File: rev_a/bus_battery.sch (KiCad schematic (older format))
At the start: 4 parts

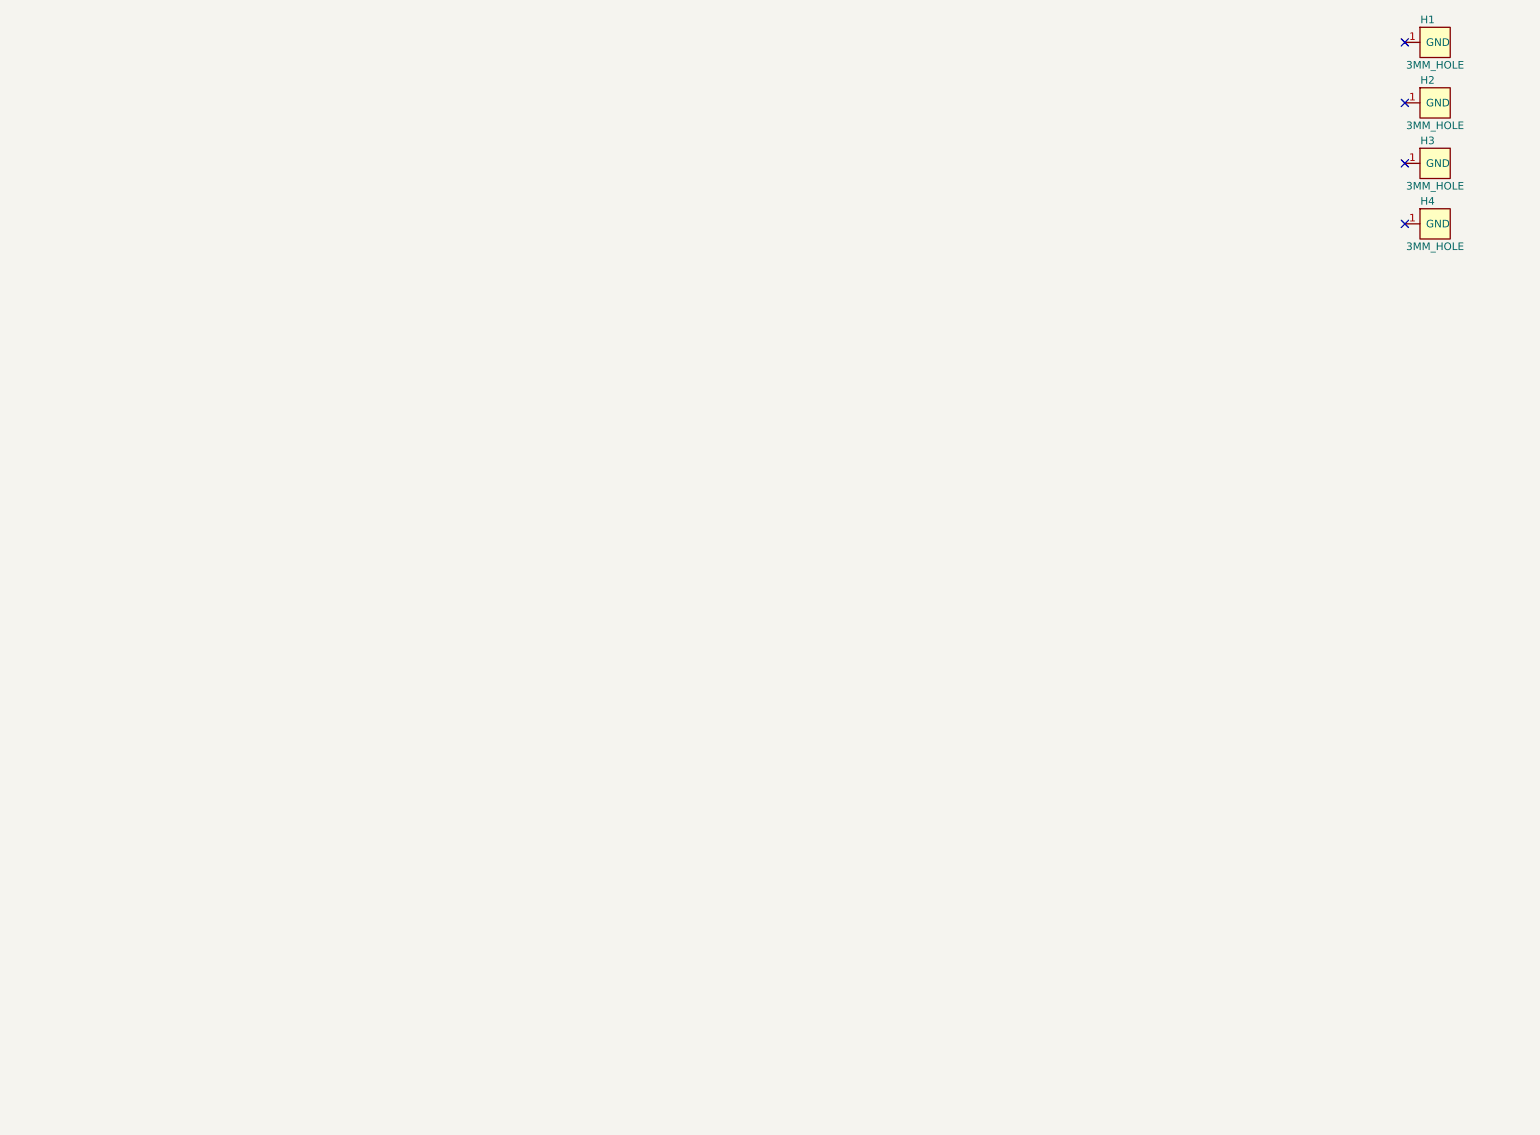
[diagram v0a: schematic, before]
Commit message: Concluded that this will have to be a 5cm x 10cm board.
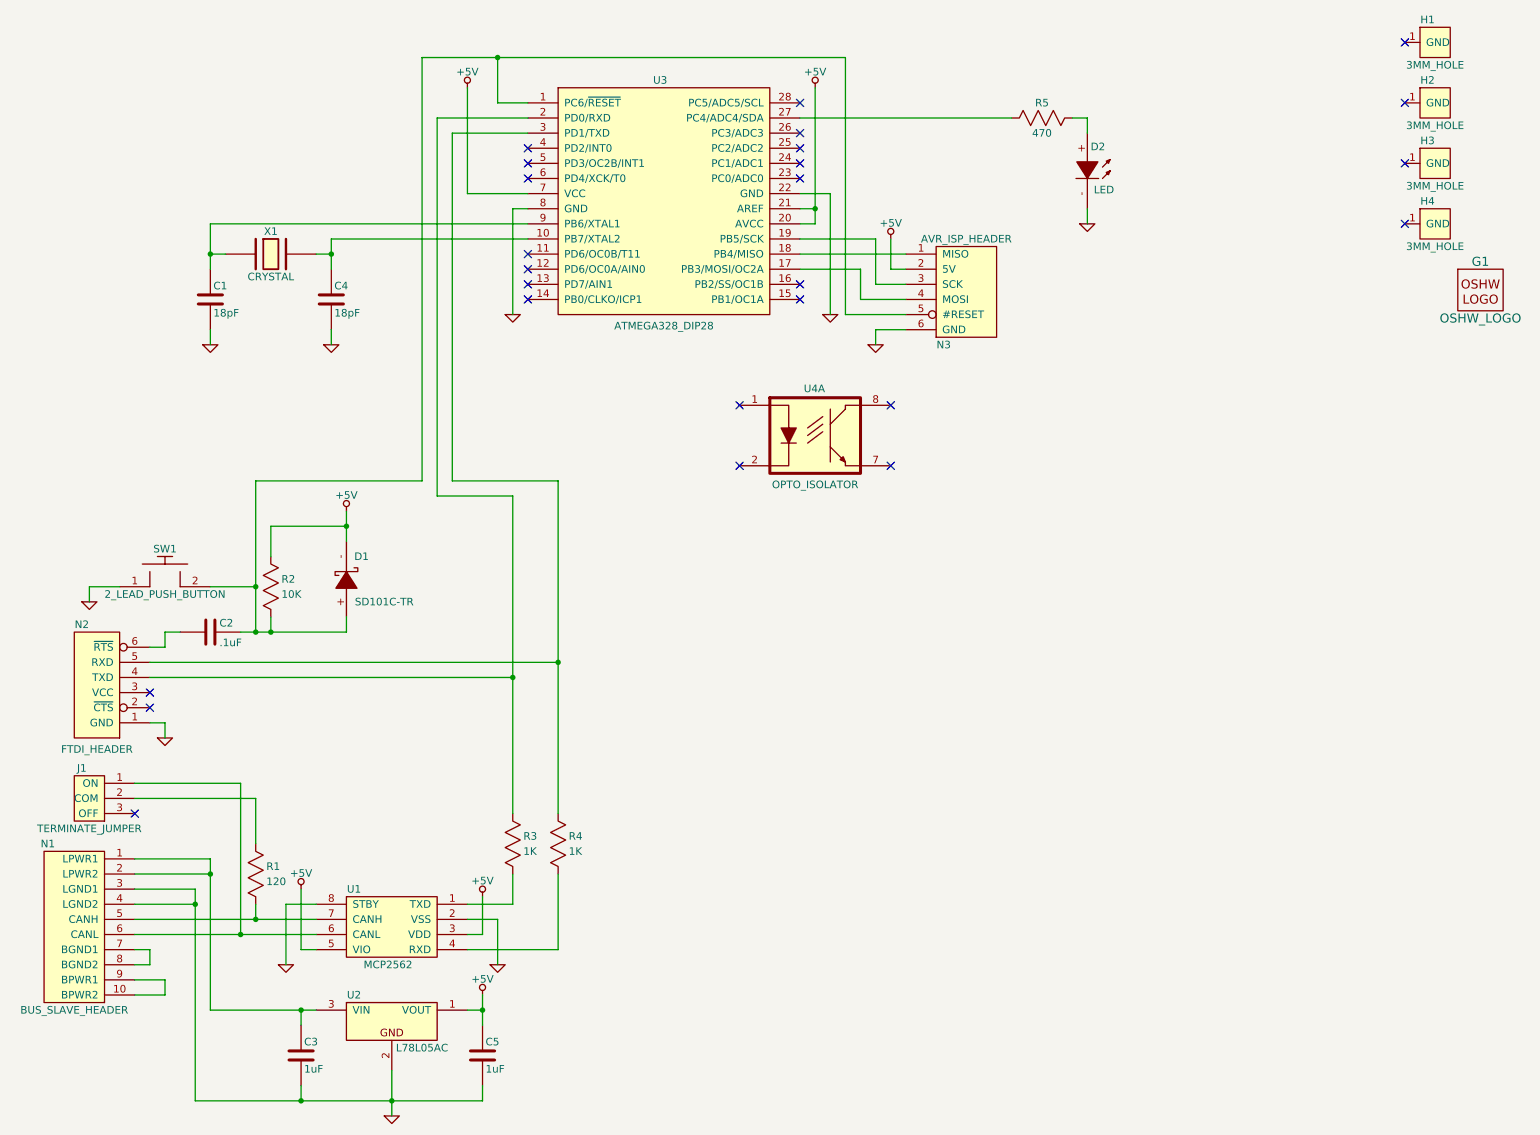
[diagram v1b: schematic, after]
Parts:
- added C1, C4: 18pF, Bus_Battery:Capacitor3MMDiscRM2.5, symbol C_VERT
- added C2: .1uF, Bus_Battery:Capacitor3MMDiscRM2.5, symbol C_HORIZ
- added C3, C5: 1uF, Bus_Battery:Capacitor3MMDiscRM2.5, symbol C_VERT
- added D1: SD101C-TR, Bus_Battery:Diode_DO-41_SOD81_Horizontal_RM10, symbol SCHOTTKY_DIODE_VERT
- added D2: LED, Bus_Battery:T1_LED, symbol LED
- added G1: OSHW_LOGO, Bus_Battery:OSHW_LOGO_250mil, symbol OSHW_LOGO
- added J1: TERMINATE_JUMPER, Bus_Battery:Pin_Header_Straight_1x03, symbol TERMINATE_JUMPER
- added N1: BUS_SLAVE_HEADER, Bus_Battery:Pin_Header_Straight_2x05_Shrouded, symbol BUS_SLAVE_HEADER
- added N2: FTDI_HEADER, Bus_Battery:Pin_Header_Straight_1x06, symbol FTDI_HEADER
- added N3: AVR_ISP_HEADER, Bus_Battery:Pin_Header_Straight_2x03, symbol AVR_ISP_HEADER
- added R1: 120, Bus_Battery:Resistor_Horizontal_RM10mm, symbol R_VERT
- added R2: 10K, Bus_Battery:Resistor_Horizontal_RM10mm, symbol R_VERT
- added R3, R4: 1K, Bus_Battery:Resistor_Horizontal_RM10mm, symbol R_VERT
- added R5: 470, Bus_Battery:Resistor_Horizontal_RM10mm, symbol R_HORIZ
- added SW1: 2_LEAD_PUSH_BUTTON, Bus_Battery:Button_6.5MM, symbol 2_LEAD_PUSH_BUTTON
- added U1: MCP2562, Bus_Battery:DIP-8__300, symbol MCP2562
- added U2: L78L05AC, Bus_Battery:TO92_123, symbol REGULATOR_321
- added U3: ATMEGA328_DIP28, Bus_Battery:DIP-28__300, symbol ATMEGA328_DIP28
- added U4: OPTO_ISOLATOR, Bus_Battery:DIP-8__300, symbol OPTO_ISOLATOR
- added X1: CRYSTAL, Bus_Battery:Crystal_HC49-U_Vertical, symbol CRYSTAL
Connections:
- new net: C2.2, D1.+, N3.5 (#RESET), R2.1, SW1.2, U3.1 (PC6/~RESET)
- new net: C4.1, U3.10 (PB7/XTAL2), X1.2
- new net: N3.4 (MOSI), U3.17 (PB3/MOSI/OC2A)
- new net: N3.1 (MISO), U3.18 (PB4/MISO)
- new net: N3.3 (SCK), U3.19 (PB5/SCK)
- new net: N2.4 (TXD), R3.2, U3.2 (PD0/RXD)
- new net: R5.1, U3.27 (PC4/ADC4/SDA)
- new net: N2.5 (RXD), R4.2, U3.3 (PD1/TXD)
- new net: C1.1, U3.9 (PB6/XTAL1), X1.1
- new net: C3.1, N1.1 (LPWR1), N1.2 (LPWR2), U2.3 (VIN)
- new net: N1.10 (BPWR2), N1.9 (BPWR1)
- new net: N1.5 (CANH), R1.1, U1.7 (CANH)
- new net: J1.1 (ON), N1.6 (CANL), U1.6 (CANL)
- new net: N1.7 (BGND1), N1.8 (BGND2)
- new net: R3.1, U1.1 (TXD)
- new net: R4.1, U1.4 (RXD)
- new net: J1.2 (COM), R1.2
- new net: C2.1, N2.6 (~RTS)
- new net: D2.+, R5.2
- new net +5V: C5.1, D1.-, N3.2 (5V), R2.2, U1.3 (VDD), U1.5 (VIO), U2.1 (VOUT), U3.20 (AVCC), U3.21 (AREF), U3.7 (VCC)
- new net GND: C1.2, C3.2, C4.2, C5.2, D2.-, N1.3 (LGND1), N1.4 (LGND2), N2.1 (GND), N3.6 (GND), SW1.1, U1.2 (VSS), U1.8 (STBY), U2.2, U3.22 (GND), U3.8 (GND)
- no-connect marks 4 -> 25

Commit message: Finished off Rev. A.
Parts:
- added C10, C6, C7, C8: .1uF, Bus_Battery:Capacitor3MMDiscRM2.5, symbol C_VERT
- added C9: .1uF, Bus_Battery:Capacitor3MMDiscRM2.5, symbol C_HORIZ
- added R10, R5: 82K, Bus_Battery:R_HORIZ_300, symbol R_VERT
- added R11, R6: 10K, Bus_Battery:R_HORIZ_300, symbol R_VERT
- added R7: 220, Bus_Battery:Pin_Header_Straight_1x06, symbol R_VERT_ISO_SIP6
- added R8: 470, Bus_Battery:R_HORIZ_300, symbol R_VERT
- added U3: L78L33AC, Bus_Battery:TO92_123, symbol REGULATOR_321
- added U4: LTV-816, Bus_Battery:DIP-8__300, symbol OPTO_ISOLATOR
- added unit 2 of U6
- added U7: MCP6321_DIP8, Bus_Battery:DIP-8__300, symbol MCP6321_DIP8
- G1: footprint Bus_Battery:OSHW_LOGO_250mil -> Bus_Battery:OSHW_LOGO_150mil
- R1: renamed from R2; footprint Bus_Battery:Resistor_Horizontal_RM10mm -> Bus_Battery:R_HORIZ_300
- R2: renamed from R1; footprint Bus_Battery:Resistor_Horizontal_RM10mm -> Bus_Battery:R_HORIZ_300
- R3: footprint Bus_Battery:Resistor_Horizontal_RM10mm -> Bus_Battery:R_HORIZ_300
- R4: value 1K -> 470; footprint Bus_Battery:Resistor_Horizontal_RM10mm -> Bus_Battery:R_HORIZ_300
- R9: renamed from R5; footprint Bus_Battery:Resistor_Horizontal_RM10mm -> Bus_Battery:R_HORIZ_300
- U6: renamed from U4; value OPTO_ISOLATOR -> LTV-816; footprint Bus_Battery:DIP-8__300 -> ~
- renumbered C2 to C1, C1 to C2, U2 to U1, U1 to U2, U3 to U5
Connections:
- net +5V: now also U3.3 (VIN), U6.3; no longer D1.-, N3.2 (5V), R1.2, U2.5 (VIO), U5.20 (AVCC), U5.21 (AREF), U5.7 (VCC)
- net GND: now also R4.1, C10.2, C6.2, C7.2, R6.1, R7.1 (6), R8.1, U3.2
- net ~RESET: now reaches C1.2, D1.+, N3.5 (#RESET), R1.1, SW1.2, U5.1 (PC6/~RESET)
- net at U5.15 (PB1/OC1A): now also U4.1
- net at U5.16 (PB2/SS/OC1B): now also U4.3
- net LVOLT: now reaches U5.23 (PC0/ADC0)
- net LVOLT: now also R5.1, R6.2
- net BVOLT: now reaches U5.24 (PC1/ADC1)
- net BVOLT: now also R7.2 (5), U6.4
- net at N2.5 (RXD), U5.3 (PD1/TXD): now also U2.1 (TXD); no longer R4.2
- net LPWR: now reaches C3.1, N1.1 (LPWR1), N1.2 (LPWR2), U1.3 (VIN)
- net LPWR: now also U4.8
- net BPWR: now reaches N1.10 (BPWR2), N1.9 (BPWR1)
- net BPWR: now also U4.6
- net BGND: now reaches N1.7 (BGND1), N1.8 (BGND2)
- net BGND: now also C8.2, R11.1, R7.6, U6.5, U7.4 (VSS)
- net at R3.1: now also U2.4 (RXD); no longer U2.1 (TXD)
- net SW_BPWR: now reaches U6.1
- net SW_BPWR: now also C8.1, R10.2, U4.5, U7.7 (VDD)
- net at U6.2: now also C9.2, R7.5, U7.2 (-)
- net at U6.7: now also U6.6
- net at U6.8: now also R7.3 (6)
- new net: R10.1, R11.2, U7.3 (+)
- new net: C9.1, R7.4 (5), U7.6 (VOUT)
- new net: R8.2, U4.4
- new net: R4.2, U4.2
- new net +3.3V: C10.1, C6.1, C7.1, D1.-, N3.2 (5V), R1.2, U2.5 (VIO), U3.1 (VOUT), U5.20 (AVCC), U5.21 (AREF), U5.7 (VCC)
- new net SW_LPWR: R5.2, U4.7
- no-connect marks 25 -> 17
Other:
- moved on the sheet: C1, C3, C5, D1, G1, J1, N1, N2, N3, R1, R2, SW1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

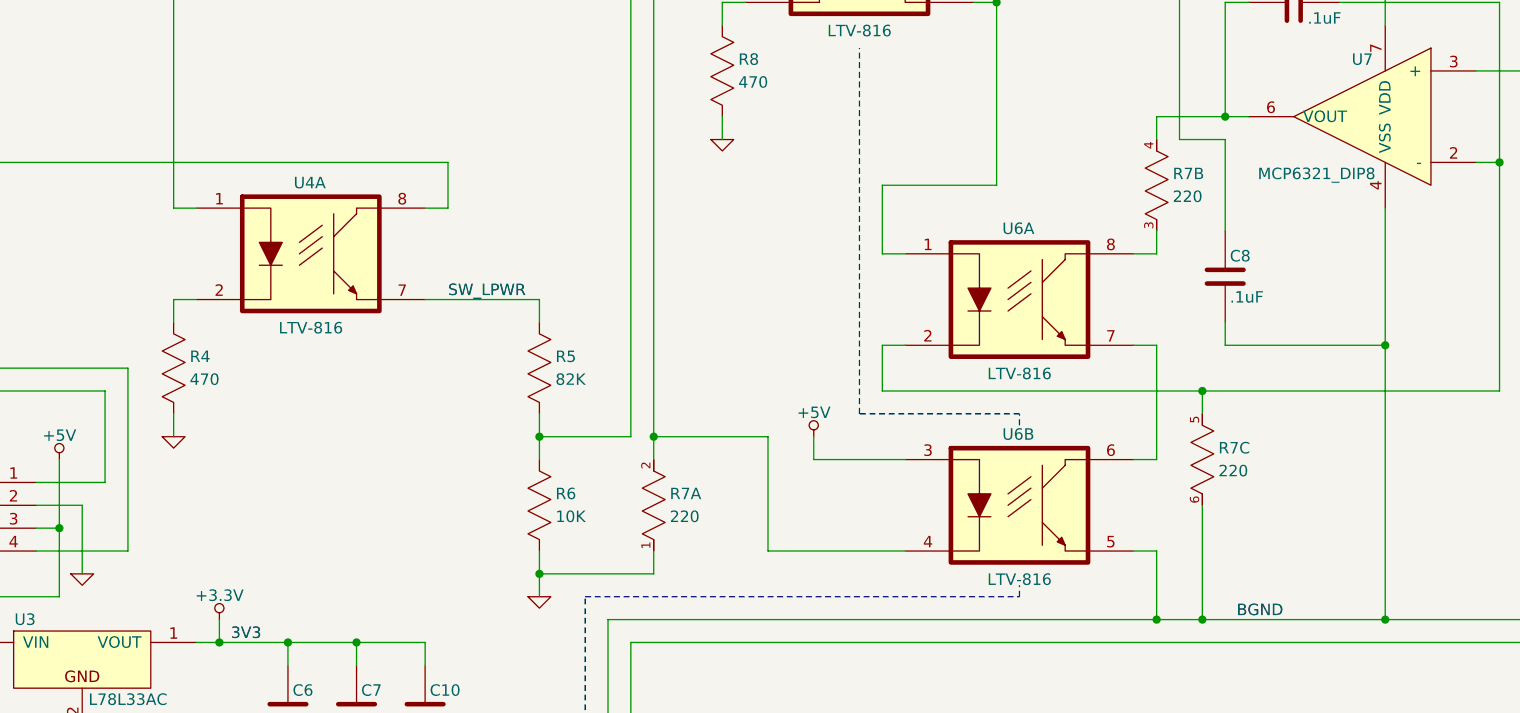
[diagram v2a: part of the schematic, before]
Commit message: Split 22uF capacitor into Aluminum and Tantulum.
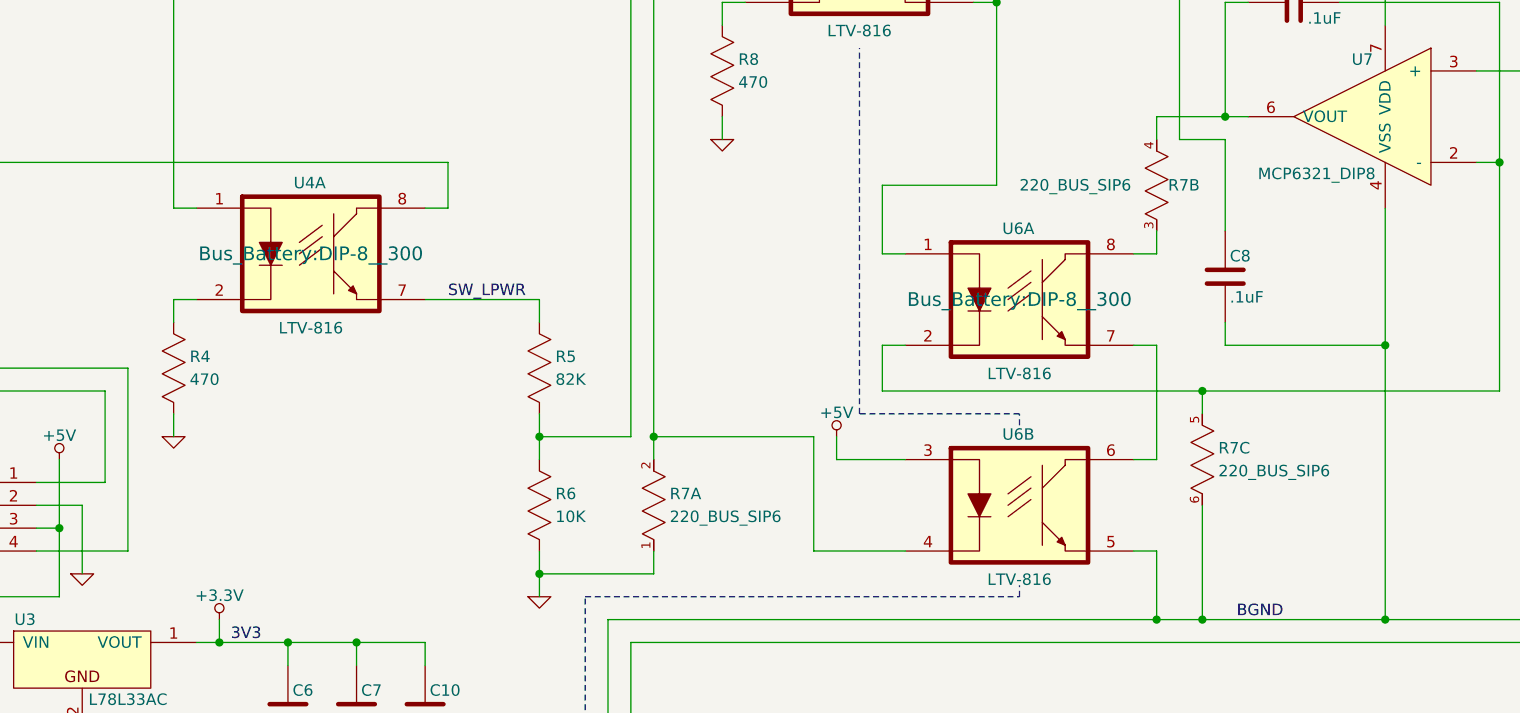
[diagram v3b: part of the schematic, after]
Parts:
- R7: value 220 -> 220_BUS_SIP6
- U4, U6: footprint ~ -> Bus_Battery:DIP-8__300
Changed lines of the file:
@@
 F 0 "U6" H 7795 5510 50  0000 C CNN
 F 1 "LTV-816" H 7800 4875 50  0000 C CNN
-F 2 "~" H 7800 5200 60  0000 C CNN
+F 2 "Bus_Battery:DIP-8__300" H 7800 5200 60  0000 C CNN
 F 3 "" H 7800 5200 60  0000 C CNN
 	1    7800 5200
@@
 L +5V #PWR018
 U 1 1 54C6D277
-P 6900 5800
-F 0 "#PWR018" H 6900 5890 20  0001 C CNN
-F 1 "+5V" H 6900 5905 50  0000 C CNN
-F 2 "" H 6900 5800 60  0000 C CNN
-F 3 "" H 6900 5800 60  0000 C CNN
-	1    6900 5800
+P 7000 5800
+F 0 "#PWR018" H 7000 5890 20  0001 C CNN
+F 1 "+5V" H 7000 5905 50  0000 C CNN
+F 2 "" H 7000 5800 60  0000 C CNN
+F 3 "" H 7000 5800 60  0000 C CNN
+	1    7000 5800
 	1    0    0    -1
 $EndComp
@@
 F 0 "U4" H 4695 5310 50  0000 C CNN
 F 1 "LTV-816" H 4700 4675 50  0000 C CNN
-F 2 "~" H 4700 5000 60  0000 C CNN
+F 2 "Bus_Battery:DIP-8__300" H 4700 5000 60  0000 C CNN
 F 3 "" H 4700 5000 60  0000 C CNN
 	1    4700 5000
@@
 P 6200 6100
 F 0 "R7" H 6270 6150 50  0000 L CNN
-F 1 "220" H 6270 6050 50  0000 L CNN
+F 1 "220_BUS_SIP6" H 6270 6050 50  0000 L CNN
 F 2 "Bus_Battery:Pin_Header_Straight_1x06" H 6200 6150 60  0001 C CNN
 F 3 "" H 6200 6150 60  0000 C CNN
@@
 U 2 1 54C6CF5C
 P 8400 4700
-F 0 "R7" H 8470 4750 50  0000 L CNN
-F 1 "220" H 8470 4650 50  0000 L CNN
+F 0 "R7" H 8450 4700 50  0000 L CNN
+F 1 "220_BUS_SIP6" H 7800 4700 50  0000 L CNN
 F 2 "Bus_Battery:Pin_Header_Straight_1x06" H 8400 4750 60  0001 C CNN
 F 3 "" H 8400 4750 60  0000 C CNN
@@
 P 8600 5900
 F 0 "R7" H 8670 5950 50  0000 L CNN
-F 1 "220" H 8670 5850 50  0000 L CNN
+F 1 "220_BUS_SIP6" H 8670 5850 50  0000 L CNN
 F 2 "Bus_Battery:Pin_Header_Straight_1x06" H 8600 5950 60  0001 C CNN
 F 3 "" H 8600 5950 60  0000 C CNN
@@
 Connection ~ 8600 5600
 Wire Wire Line
-	7300 6300 6700 6300
-Wire Wire Line
-	7300 5900 6900 5900
-Wire Wire Line
-	6900 5900 6900 5800
+	7300 6300 6900 6300
+Wire Wire Line
+	7300 5900 7000 5900
+Wire Wire Line
+	7000 5900 7000 5800
 Wire Wire Line
 	2900 3800 2900 900
@@
 	6200 1600 6200 5900
 Wire Wire Line
-	6200 5800 6700 5800
-Wire Wire Line
-	6700 5800 6700 6300
+	6200 5800 6900 5800
+Wire Wire Line
+	6900 5800 6900 6300
 Wire Wire Line
 	5800 3500 5800 2500
